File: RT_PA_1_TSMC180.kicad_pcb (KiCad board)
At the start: 2 copper layers, 86 parts, among them J1 Conn_Coaxial, J14 Conn_01x02_Female, J15 Conn_01x02_Female, J17 Conn_01x03, J20 Conn_01x01, J21 Conn_01x01, J22 Conn_01x01, J23 Conn_01x01, J24 Conn_01x01, J25 Conn_01x01, J26 Conn_01x01, J29 Conn_Coaxial, J3 Conn_Coaxial, J31 Conn_Coaxial, J33 Conn_Coaxial, J35 Conn_Coaxial, J37 Conn_Coaxial, J39 Conn_Coaxial, J401 Conn_01x02, J41 Conn_Coaxial, J43 Conn_Coaxial, J49 Conn_01x04, J5 Conn_Coaxial, J50 Conn_01x04, J55 Conn_01x02, J56 Conn_01x02, J57 Conn_01x02, J58 Conn_01x03, J60 Conn_01x02, J61 Conn_01x02, J62 Conn_01x03, J65 Conn_Coaxial, J67 Conn_Coaxial, J7 Conn_Coaxial, J9 Conn_01x02_Female, SW1 SW_DIP_x03, SW10 SW_DIP_x03, SW11 SW_DIP_x02, SW12 SW_DIP_x04, SW13 SW_DIP_x04, SW14 SW_DIP_x04, SW15 SW_DIP_x04, SW2 SW_DIP_x03, SW3 SW_DIP_x03, SW4 SW_DIP_x02, SW5 SW_DIP_x02, SW6 SW_DIP_x01, SW7 SW_DIP_x02, SW8 SW_DIP_x02, SW9 SW_DIP_x02, U1 PART1p68

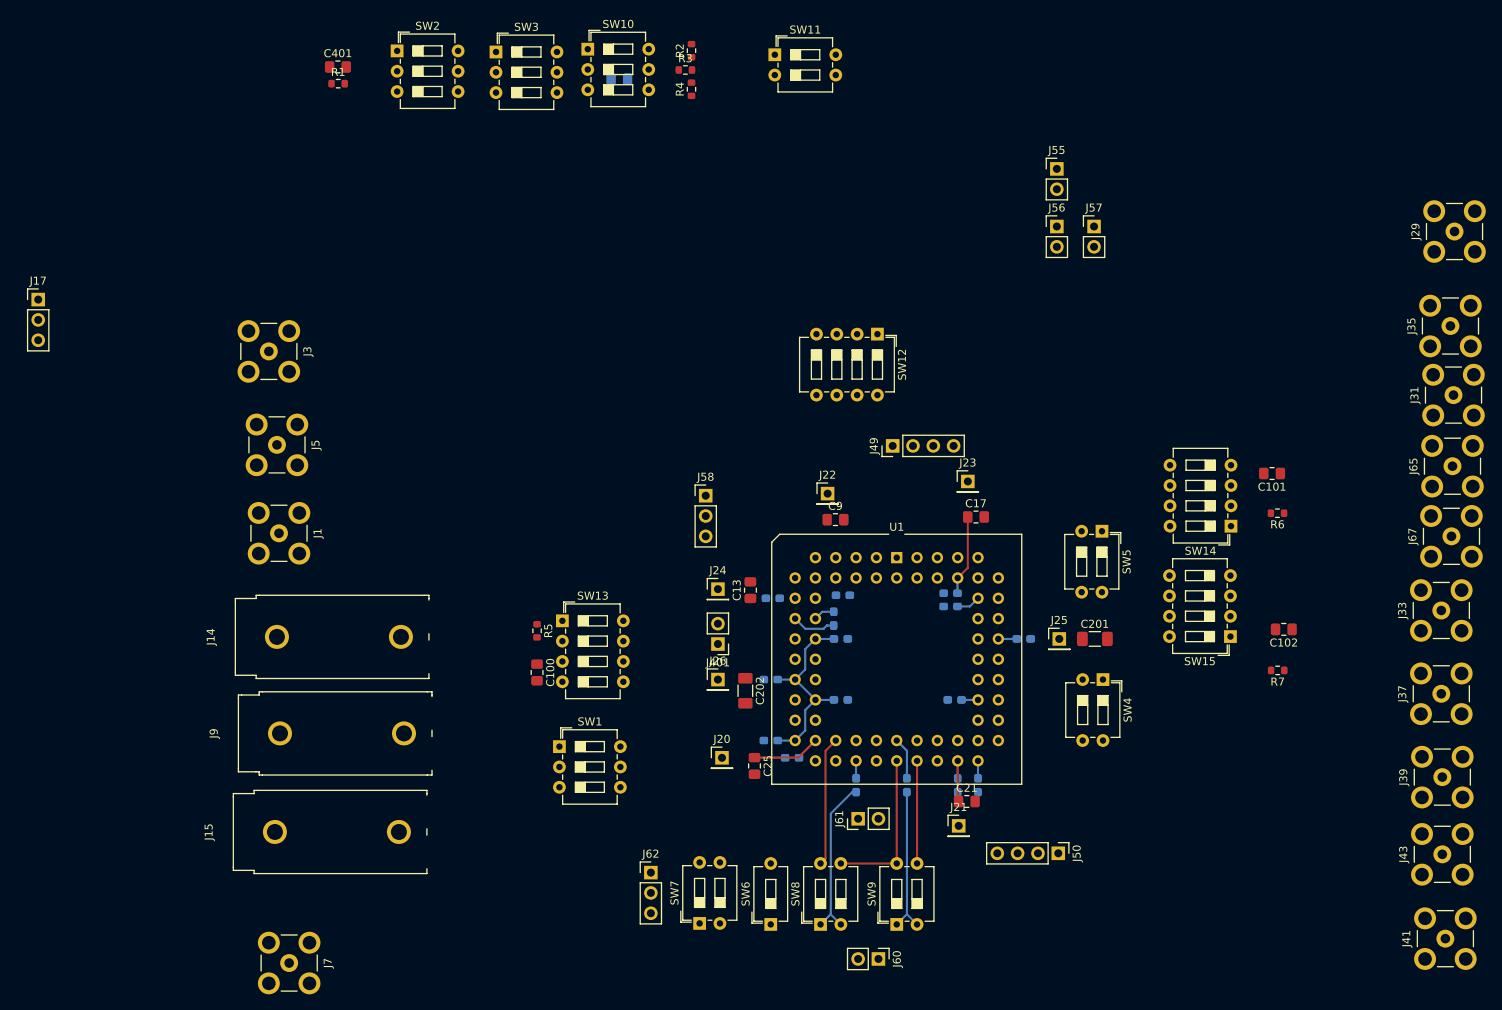
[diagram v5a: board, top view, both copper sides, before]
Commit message: PCB layout complete, ready for review.
Signed-off-by: Alexis Jeandet <alexis.jeandet@member.fsf.org>
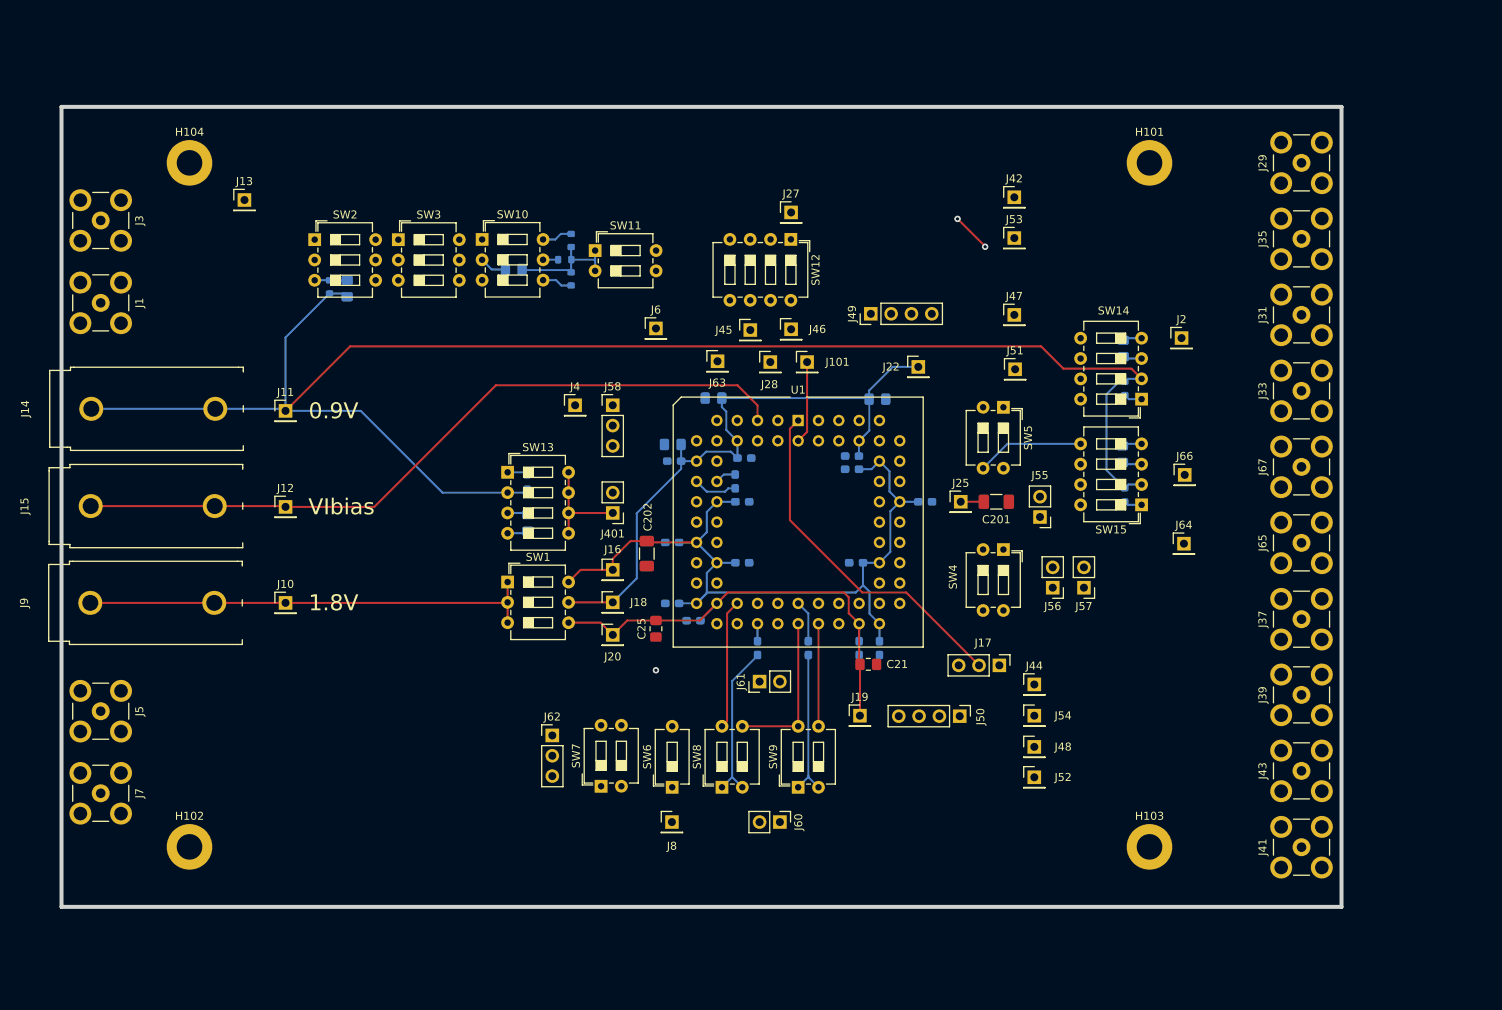
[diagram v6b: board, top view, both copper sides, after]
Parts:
- removed J21, J23, J24, J26: Conn_01x01, Connector_PinHeader_2.54mm:PinHeader_1x01_P2.54mm_Vertical
- added H101: MountingHole_Pad, MountingHole:MountingHole_3.2mm_M3_ISO7380_Pad, F.Cu at (200.0, 60.0)
- added H102: MountingHole_Pad, MountingHole:MountingHole_3.2mm_M3_ISO7380_Pad, F.Cu at (80.0, 145.5)
- added H103: MountingHole_Pad, MountingHole:MountingHole_3.2mm_M3_ISO7380_Pad, F.Cu at (200.0, 145.5)
- added H104: MountingHole_Pad, MountingHole:MountingHole_3.2mm_M3_ISO7380_Pad, F.Cu at (80.0, 60.0)
- added J10: Conn_01x01, Connector_PinHeader_2.54mm:PinHeader_1x01_P2.54mm_Vertical, F.Cu at (92.0, 115.0)
- added J101: Conn_01x01, Connector_PinHeader_2.54mm:PinHeader_1x01_P2.54mm_Vertical, F.Cu at (157.2, 84.9)
- added J11: Conn_01x01, Connector_PinHeader_2.54mm:PinHeader_1x01_P2.54mm_Vertical, F.Cu at (92.0, 91.0)
- added J12: Conn_01x01, Connector_PinHeader_2.54mm:PinHeader_1x01_P2.54mm_Vertical, F.Cu at (92.0, 103.0)
- added J13: Conn_01x01, Connector_PinHeader_2.54mm:PinHeader_1x01_P2.54mm_Vertical, F.Cu at (86.9, 64.6)
- added J16: Conn_01x01, Connector_PinHeader_2.54mm:PinHeader_1x01_P2.54mm_Vertical, F.Cu at (132.9, 110.9)
- added J18: Conn_01x01, Connector_PinHeader_2.54mm:PinHeader_1x01_P2.54mm_Vertical, F.Cu at (132.9, 114.9)
- added J19: Conn_01x01, Connector_PinHeader_2.54mm:PinHeader_1x01_P2.54mm_Vertical, F.Cu at (163.8, 129.1)
- added J2: Conn_01x01, Connector_PinHeader_2.54mm:PinHeader_1x01_P2.54mm_Vertical, F.Cu at (204.0, 81.9)
- added J27: Conn_01x01, Connector_PinHeader_2.54mm:PinHeader_1x01_P2.54mm_Vertical, F.Cu at (155.2, 66.2)
- added J28: Conn_01x01, Connector_PinHeader_2.54mm:PinHeader_1x01_P2.54mm_Vertical, F.Cu at (152.6, 84.9)
- added J4: Conn_01x01, Connector_PinHeader_2.54mm:PinHeader_1x01_P2.54mm_Vertical, F.Cu at (128.2, 90.3)
- added J42: Conn_01x01, Connector_PinHeader_2.54mm:PinHeader_1x01_P2.54mm_Vertical, F.Cu at (183.1, 64.3)
- added J44: Conn_01x01, Connector_PinHeader_2.54mm:PinHeader_1x01_P2.54mm_Vertical, F.Cu at (185.6, 125.2)
- added J45: Conn_01x01, Connector_PinHeader_2.54mm:PinHeader_1x01_P2.54mm_Vertical, F.Cu at (150.1, 80.9)
- added J46: Conn_01x01, Connector_PinHeader_2.54mm:PinHeader_1x01_P2.54mm_Vertical, F.Cu at (155.2, 80.8)
- added J47: Conn_01x01, Connector_PinHeader_2.54mm:PinHeader_1x01_P2.54mm_Vertical, F.Cu at (183.1, 79.0)
- added J48: Conn_01x01, Connector_PinHeader_2.54mm:PinHeader_1x01_P2.54mm_Vertical, F.Cu at (185.6, 133.0)
- added J51: Conn_01x01, Connector_PinHeader_2.54mm:PinHeader_1x01_P2.54mm_Vertical, F.Cu at (183.2, 85.8)
- added J52: Conn_01x01, Connector_PinHeader_2.54mm:PinHeader_1x01_P2.54mm_Vertical, F.Cu at (185.6, 136.8)
- added J53: Conn_01x01, Connector_PinHeader_2.54mm:PinHeader_1x01_P2.54mm_Vertical, F.Cu at (183.1, 69.4)
- added J54: Conn_01x01, Connector_PinHeader_2.54mm:PinHeader_1x01_P2.54mm_Vertical, F.Cu at (185.6, 129.1)
- added J6: Conn_01x01, Connector_PinHeader_2.54mm:PinHeader_1x01_P2.54mm_Vertical, F.Cu at (138.3, 80.7)
- added J63: Conn_01x01, Connector_PinHeader_2.54mm:PinHeader_1x01_P2.54mm_Vertical, F.Cu at (146.0, 84.8)
- added J64: Conn_01x01, Connector_PinHeader_2.54mm:PinHeader_1x01_P2.54mm_Vertical, F.Cu at (204.3, 107.6)
- added J66: Conn_01x01, Connector_PinHeader_2.54mm:PinHeader_1x01_P2.54mm_Vertical, F.Cu at (204.4, 99.0)
- added J8: Conn_01x01, Connector_PinHeader_2.54mm:PinHeader_1x01_P2.54mm_Vertical, F.Cu at (140.3, 142.4)
- C100, C101, C102, C13, C17, C401, C9, R1, R2, R3, R4, R5, R6, R7: moved to B.Cu
- J14, J15, J9: value Conn_01x02_Female -> Conn_01x01_Female
- moved J17 128.5 mm to (181.2, 122.8), turned to 270 degrees
- moved J15 46.8 mm to (75.4, 102.9)
- moved J57 45.2 mm to (191.8, 113.1), turned to 180 degrees
- moved J56 45.1 mm to (187.9, 113.1), turned to 180 degrees
- moved J55 43.6 mm to (186.3, 104.3), turned to 180 degrees
- moved J5 39.9 mm to (68.9, 128.5)
- moved J14 36.8 mm to (75.5, 90.7)
- moved J1 36.4 mm to (68.9, 77.5)
- moved SW11 33.2 mm to (130.7, 71.0)
- moved J33 32.5 mm to (219.0, 88.5)
- moved J7 31.7 mm to (68.9, 138.8)
- moved C102 29.8 mm to (196.6, 96.4), turned to 90 degrees
- moved R7 29.1 mm to (196.9, 101.5), turned to 90 degrees
- moved J9 28.8 mm to (75.3, 115.0)
- moved R3 28.1 mm to (126.9, 72.1)
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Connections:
- J15 pad 1: /1V14_g -> /VIbias
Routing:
- net /Vin: track 0.00 -> 235.2 mm, vias 0 -> 2
- net /0V9_g: track 0.00 -> 210.6 mm
- net /VoO: track 0.00 -> 140.1 mm, vias 0 -> 1
- net /VIbias: track 0.00 -> 126.9 mm
- net /VoOi: track 0.00 -> 113.2 mm
- net /VoM: track 0.00 -> 111.1 mm
- net /Vi1O: track 0.00 -> 108.8 mm
- net /Vi1m: track 0.00 -> 104.7 mm
- net /Vi2m: track 0.00 -> 86.2 mm
- net /pS: track 0.00 -> 79.6 mm
- net /pD: track 0.00 -> 75.9 mm
- net /VDD_diff: track 34.4 -> 108.9 mm
- net /nG: track 0.00 -> 74.4 mm
- net /nS: track 0.00 -> 73.4 mm
- net /pB: track 0.00 -> 72.4 mm
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- added copper zone on B.Cu, net GND
- added copper zone on F.Cu, net GND
- added copper zone on In1.Cu, net GND
- added copper zone on In2.Cu, net GND
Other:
- board outline added: 160 x 100 mm
- copper layers 2 -> 4
- board text added: "0.9V"
- board text added: "1.8V"
- board text added: "VIbias"

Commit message: Some modifications on schematic and Layout to be optimised!
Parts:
- removed J17: Conn_01x03, Connector_PinHeader_2.54mm:PinHeader_1x03_P2.54mm_Vertical
- added J171: Conn_01x01, Connector_PinHeader_2.54mm:PinHeader_1x01_P2.54mm_Vertical, F.Cu at (181.6, 121.9)
- added J172: Conn_01x01, Connector_PinHeader_2.54mm:PinHeader_1x01_P2.54mm_Vertical, F.Cu at (157.5, 85.1)
- added J173: Conn_01x01, Connector_PinHeader_2.54mm:PinHeader_1x01_P2.54mm_Vertical, F.Cu at (133.3, 123.2)
- added J_VDD_io: Conn_Coaxial, banana:Banana_test_point_4mm, F.Cu at (76.2, 108.0)
- moved J101 19.3 mm to (161.3, 66.0)
- moved J11 8.45 mm to (92.0, 82.5)
- moved J14 8.23 mm to (76.2, 82.5)
- moved J12 7.75 mm to (92.0, 95.2)
- moved J15 7.69 mm to (76.2, 95.2)
- moved H102 7.66 mm to (87.6, 144.8)
- moved H104 7.64 mm to (87.6, 59.7)
- moved J10 6.94 mm to (91.4, 121.9)
- moved J9 6.92 mm to (75.3, 121.9)
- moved J1 6.38 mm to (68.9, 71.1)
- moved J3 6.24 mm to (68.9, 61.0)
- moved J5 6.08 mm to (68.9, 134.6)
- moved J7 5.98 mm to (68.9, 144.8)
- moved J13 4.43 mm to (88.9, 68.6)
- renumbered SW12 to S_Bias1, SW10 to S_G1, SW11 to S_G2, SW2 to S_GiN_1, SW3 to S_GiN_2, SW8 to S_OiN_comp1, SW9 to S_OiP_comp1, SW6 to S_Ooi_SE1, SW7 to S_Ooii_SE_Diff1, SW4 to S_S2_inN1, SW5 to S_S2_inP1, SW1 to S_VDD1, SW13 to S_iCM_Diff1, SW14 to S_iCM_M1, SW15 to S_iCM_O1
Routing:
- net /VDD_io: track 0.00 -> 102.2 mm
- net /VM_O: track 38.7 -> 16.3 mm
- net /Vo1m: track 10.3 -> 30.8 mm, vias 0 -> 1
- net /VoM: track 111.1 -> 125.0 mm
- net /0V9_g: track 210.6 -> 202.0 mm, vias 0 -> 1
- net /VM_M: track 44.0 -> 51.7 mm
- net /VIbias: track 126.9 -> 122.8 mm
- net /VoOi: track 113.2 -> 115.8 mm
- net /1V8_g: track 57.3 -> 59.2 mm
- net /Vin: track 235.2 -> 236.5 mm
- net /VM_diff: track 19.0 -> 18.3 mm
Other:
- board text added: "Vi2O"
- board text added: "Vi2m"
- board text added: "Vin"
- board text added: "VoM"
- board text added: "VoO"
- board text added: "VoOi"
- board text added: "nB"
- board text added: "nD"
- board text added: "nG"
- board text added: "nS"
- board text added: "pB"
- board text added: "pD"
- board text added: "pG"
- board text added: "pS"

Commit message: PCB ready for production
Signed-off-by: Alexis Jeandet <alexis.jeandet@member.fsf.org>
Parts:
- added J201: Conn_01x01, Connector_PinHeader_2.54mm:PinHeader_1x01_P2.54mm_Vertical, F.Cu at (103.6, 144.8)
- added J202: Conn_01x01, Connector_PinHeader_2.54mm:PinHeader_1x01_P2.54mm_Vertical, F.Cu at (185.9, 145.5)
- added J203: Conn_01x01, Connector_PinHeader_2.54mm:PinHeader_1x01_P2.54mm_Vertical, F.Cu at (175.5, 60.0)
- added J402: Conn_01x01, Connector_PinHeader_2.54mm:PinHeader_1x01_P2.54mm_Vertical, F.Cu at (146.2, 126.4)
- J60: value Conn_01x02 -> Conn_01x01; footprint Connector_PinHeader_2.54mm:PinHeader_1x02_P2.54mm_Vertical -> Connector_PinHeader_2.54mm:PinHeader_1x01_P2.54mm_Vertical
- J_VDD_io501: renamed from J_VDD_io; value Conn_Coaxial -> Conn_01x01_Female
- moved J60 16.9 mm to (159.0, 126.4)
- moved J_VDD_io501 1.96 mm to (75.0, 109.5)
- moved J14 1.53 mm to (75.0, 83.5)
- moved J15 1.42 mm to (75.0, 96.0)
- moved J66 1.40 mm to (203.0, 99.0)
- moved J64 1.30 mm to (203.0, 107.6)
- moved J11 1.14 mm to (92.0, 83.7)
- moved J2 1.00 mm to (203.0, 81.9)
- moved J12 0.76 mm to (92.0, 96.0)
- moved J9 0.35 mm to (75.0, 122.0)
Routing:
- net /VM_M: track 51.7 -> 7.69 mm
- net /Vi2m: track 86.2 -> 84.6 mm
- net /VIbias: track 122.8 -> 124.3 mm
- net /VM_O: track 16.3 -> 14.8 mm
- net /nD: track 70.3 -> 71.4 mm
- net /VDD_io: track 102.2 -> 103.2 mm
- net /Vin: track 236.5 -> 235.5 mm
- net /0V9_g: track 202.0 -> 202.7 mm
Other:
- board text added: "GND"
- board text added: "On"
- board text added: "VDD_io"
